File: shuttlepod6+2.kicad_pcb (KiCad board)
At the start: 2 copper layers, 76.4 x 58 mm, 33 parts, among them K11 KEYSW, K12 KEYSW, K21 KEYSW, K22 KEYSW, K31 KEYSW, K32 KEYSW, P1 USB_C_Plug_USB2.0, SW1 SW_PUSH, U1 ATMEGA32U4, X1 XTAL_GND

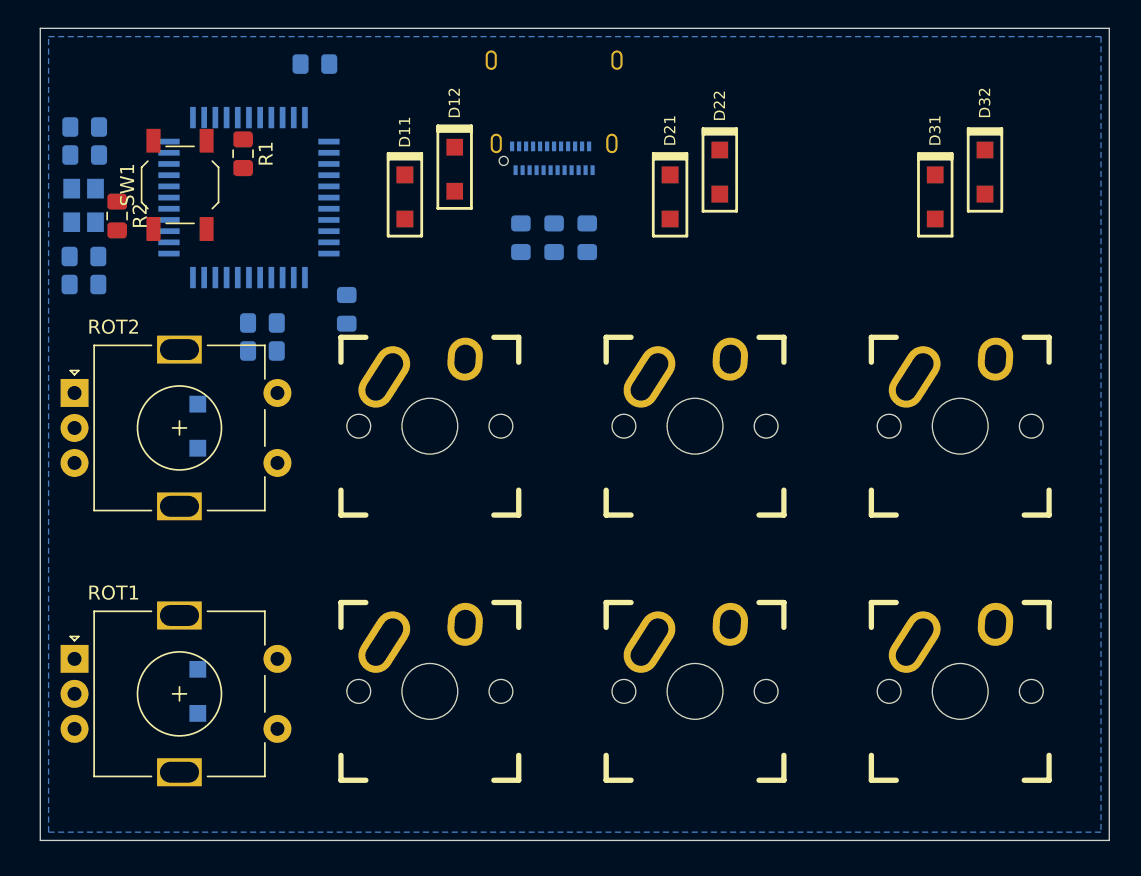
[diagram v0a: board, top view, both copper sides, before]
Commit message: changed design, got rid of bezel
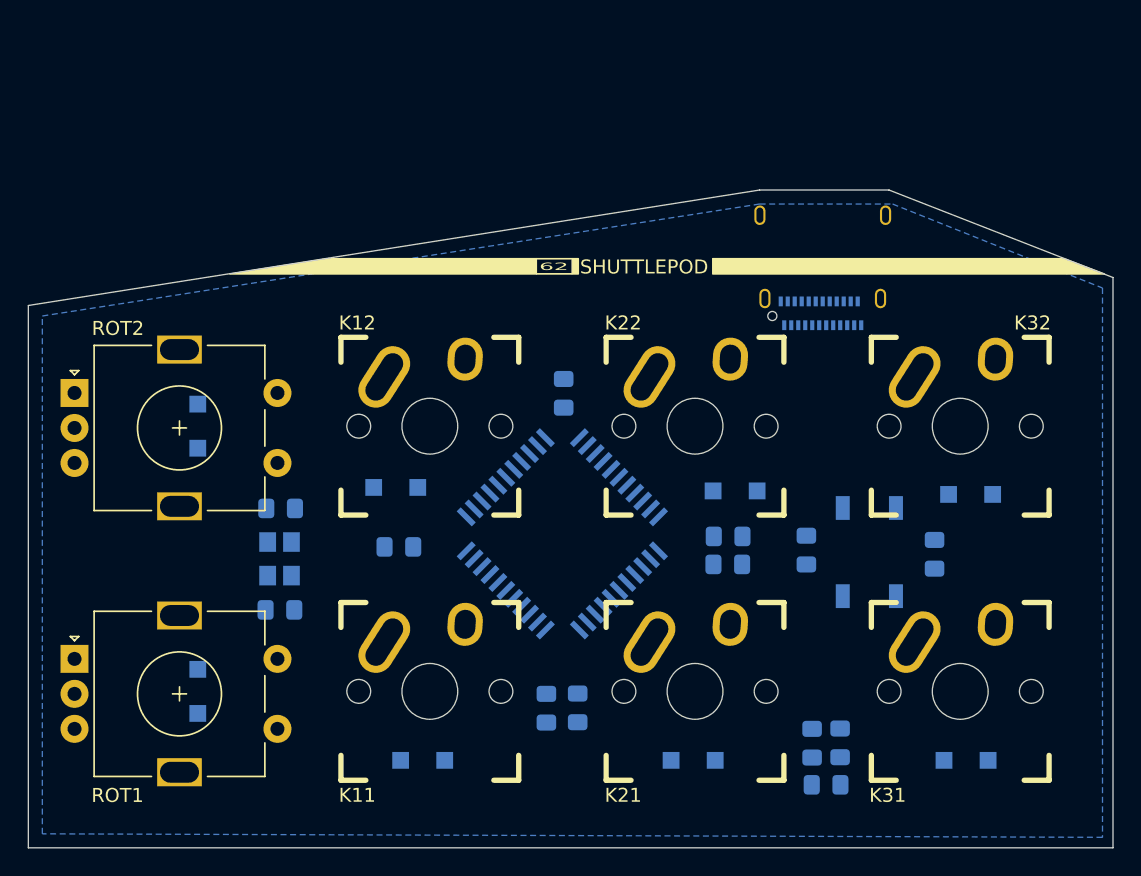
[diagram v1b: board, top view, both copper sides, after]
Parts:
- D11, D12, D21, D22, D31, D32, R1, R2, SW1: moved to B.Cu
- moved R1 57.1 mm to (104.8, 101.5), turned to 90 degrees
- moved SW1 55.8 mm to (100.1, 101.4), turned to 270 degrees
- moved R2 54.7 mm to (95.6, 101.2), turned to 90 degrees
- moved C3 44.8 mm to (90.0, 100.2), turned to 0 degrees
- moved R5 44.8 mm to (97.0, 118.0), turned to 0 degrees
- moved R3 40.5 mm to (96.0, 115.0)
- moved R4 40.4 mm to (98.0, 115.0)
- moved D31 40.3 mm to (107.0, 116.2), turned to 0 degrees
- moved D21 40.3 mm to (87.5, 116.2), turned to 0 degrees
- moved D11 40.3 mm to (68.2, 116.2), turned to 0 degrees
- moved C7 39.2 mm to (78.2, 90.0), turned to 90 degrees
- moved C8 37.5 mm to (90.0, 102.2)
- moved C6 32.9 mm to (79.2, 112.5)
- moved U1 32.8 mm to (78.2, 100.1), turned to 135 degrees
- moved C5 32.6 mm to (77.0, 112.5), turned to 270 degrees
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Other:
- board size 76.4 x 58 mm -> 77.5 x 47 mm
- board text added: "62"
- board text added: "SHUTTLEPOD"

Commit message: moved crystal closer and better cap placement
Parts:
- moved C4 16.5 mm to (77.0, 88.3), turned to 90 degrees
- moved X1 8.15 mm to (66.1, 102.0), turned to 135 degrees
- moved C2 3.98 mm to (61.5, 100.2), turned to 270 degrees
- moved C1 3.76 mm to (61.5, 104.2), turned to 90 degrees
- moved C7 2.02 mm to (79.2, 88.3)

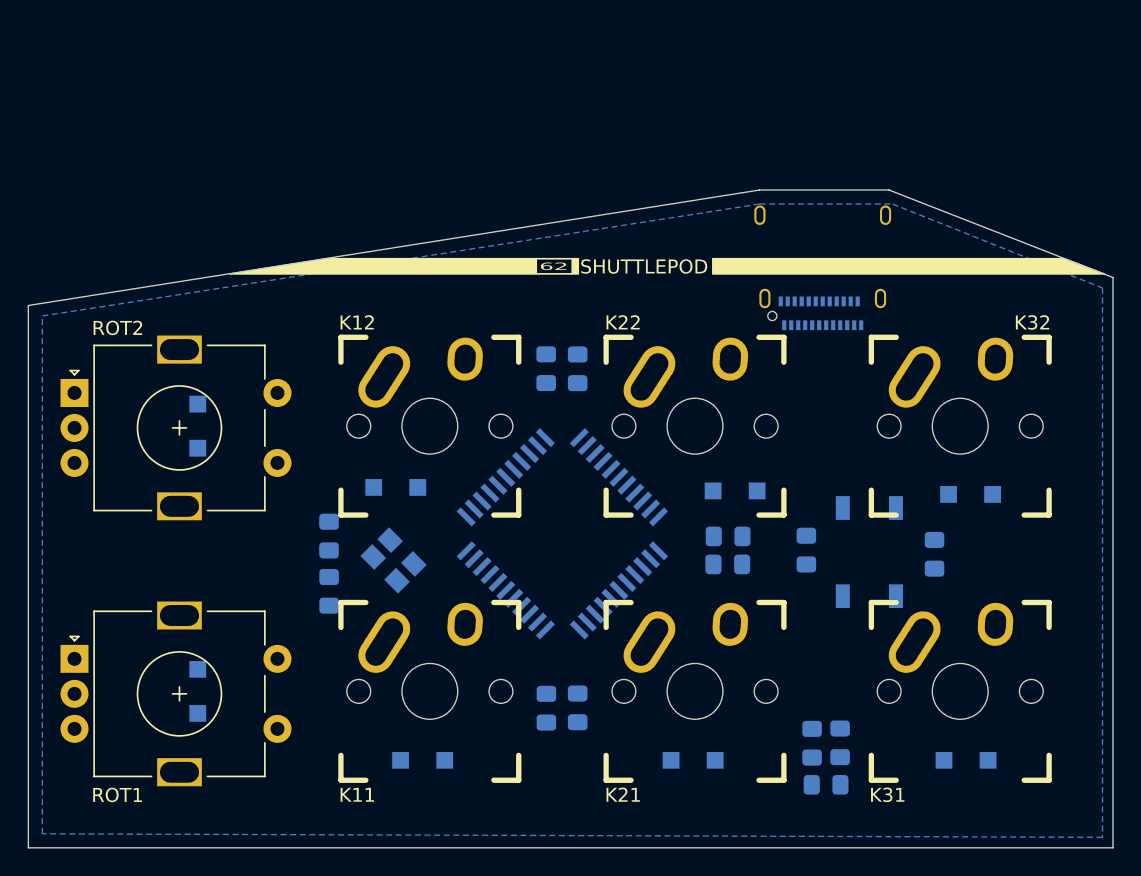
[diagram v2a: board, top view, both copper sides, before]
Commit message: first routing attempt
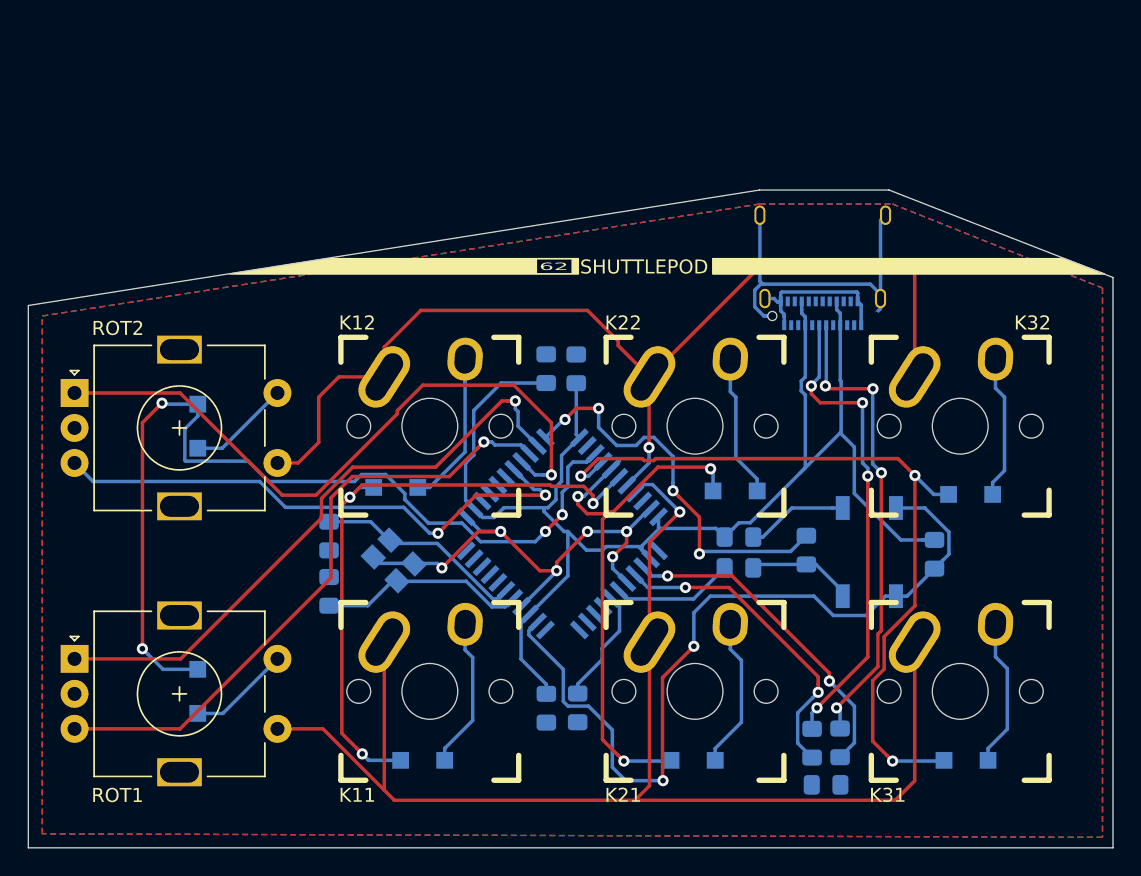
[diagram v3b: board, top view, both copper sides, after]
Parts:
- moved C7 16.7 mm to (90.8, 100.3), turned to 0 degrees
- moved C3 16.2 mm to (79.2, 88.3), turned to 90 degrees
- moved C8 0.84 mm to (90.8, 102.5)
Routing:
- net VCC: track 0.00 -> 117.8 mm
- net COL1: track 0.00 -> 94.9 mm, vias 0 -> 1
- net COL2: track 0.00 -> 75.0 mm, vias 0 -> 1
- net ROW4: track 0.00 -> 66.4 mm, vias 0 -> 4
- net GND: track 0.00 -> 62.2 mm, vias 0 -> 6
- net Net-(R1-Pad1): track 0.00 -> 58.1 mm, vias 0 -> 2
- net ROW3: track 0.00 -> 55.9 mm, vias 0 -> 3
- net Rot2+: track 0.00 -> 47.8 mm, vias 0 -> 1
- net ROW1: track 0.00 -> 45.4 mm, vias 0 -> 3
- net Rot1-: track 0.00 -> 44.7 mm, vias 0 -> 1
- net Rot1+: track 0.00 -> 43.8 mm, vias 0 -> 1
- net Rot2-: track 0.00 -> 39.9 mm, vias 0 -> 2
- net ROW2: track 0.00 -> 39.0 mm, vias 0 -> 3
- net Net-(P1-PadA6): track 0.00 -> 34.2 mm, vias 0 -> 4
- net Net-(P1-PadA7): track 0.00 -> 33.8 mm, vias 0 -> 4
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- added copper zone on F.Cu, net GND

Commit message: even better routing (or so i hope)
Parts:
- moved R5 28.2 mm to (95.2, 89.8), turned to 270 degrees
- moved R3 25.2 mm to (97.2, 89.8)
- moved R4 25.2 mm to (99.2, 89.8)
- moved D21 9.65 mm to (90.2, 107.0)
- moved D31 9.58 mm to (109.5, 107.0)
- moved D11 9.45 mm to (66.2, 107.0)
- moved C5 4.25 mm to (77.0, 116.8)
- moved C6 4.25 mm to (79.2, 116.8)
- moved C3 2.51 mm to (79.4, 90.8)
- moved C4 2.51 mm to (77.2, 90.8)
- moved U1 2.19 mm to (78.2, 102.2)
- moved C1 1.69 mm to (59.9, 104.6)
- moved C2 1.67 mm to (59.9, 99.9)
- moved C8 0.75 mm to (90.8, 103.2)
- moved C7 0.30 mm to (90.8, 100.0)
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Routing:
- net Net-(P1-PadA6): track 34.2 -> 3.93 mm, vias 4 -> 0
- net Net-(P1-PadA7): track 33.8 -> 4.52 mm, vias 4 -> 0
- net (no net): track 25.1 -> 0.00 mm
- net Net-(R1-Pad1): track 58.1 -> 38.4 mm
- net ROW2: track 39.0 -> 23.7 mm
- net ROW3: track 55.9 -> 43.3 mm, vias 3 -> 2
- net ROW4: track 66.4 -> 53.8 mm, vias 4 -> 2
- net GND: track 62.2 -> 74.7 mm
- net Rot2+: track 47.8 -> 35.4 mm
- net Rot2-: track 39.9 -> 32.5 mm, vias 2 -> 1
- net VCC: track 117.8 -> 125.0 mm, vias 0 -> 4
- net Net-(R2-Pad2): track 28.6 -> 23.2 mm, vias 4 -> 2
- net Net-(D31-Pad2): track 10.6 -> 15.7 mm
- net Net-(C2-Pad1): track 15.2 -> 20.2 mm
- net D-: track 23.7 -> 28.6 mm, vias 2 -> 0
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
